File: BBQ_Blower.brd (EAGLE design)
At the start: 84.9 x 75.9 mm, 36 parts, among them IC1 MAX31855RASA+, IC2 MAX31855RASA+, IC3 MAX31855RASA+, J3 PCC-SMP-K-100-R-ROHS, J4 PCC-SMP-K-100-R-ROHS, K1 SRD-12VDC-SL-C, K2 SRD-12VDC-SL-C, Q1 BUZ10, Q2 BUZ10, T1 2N3904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

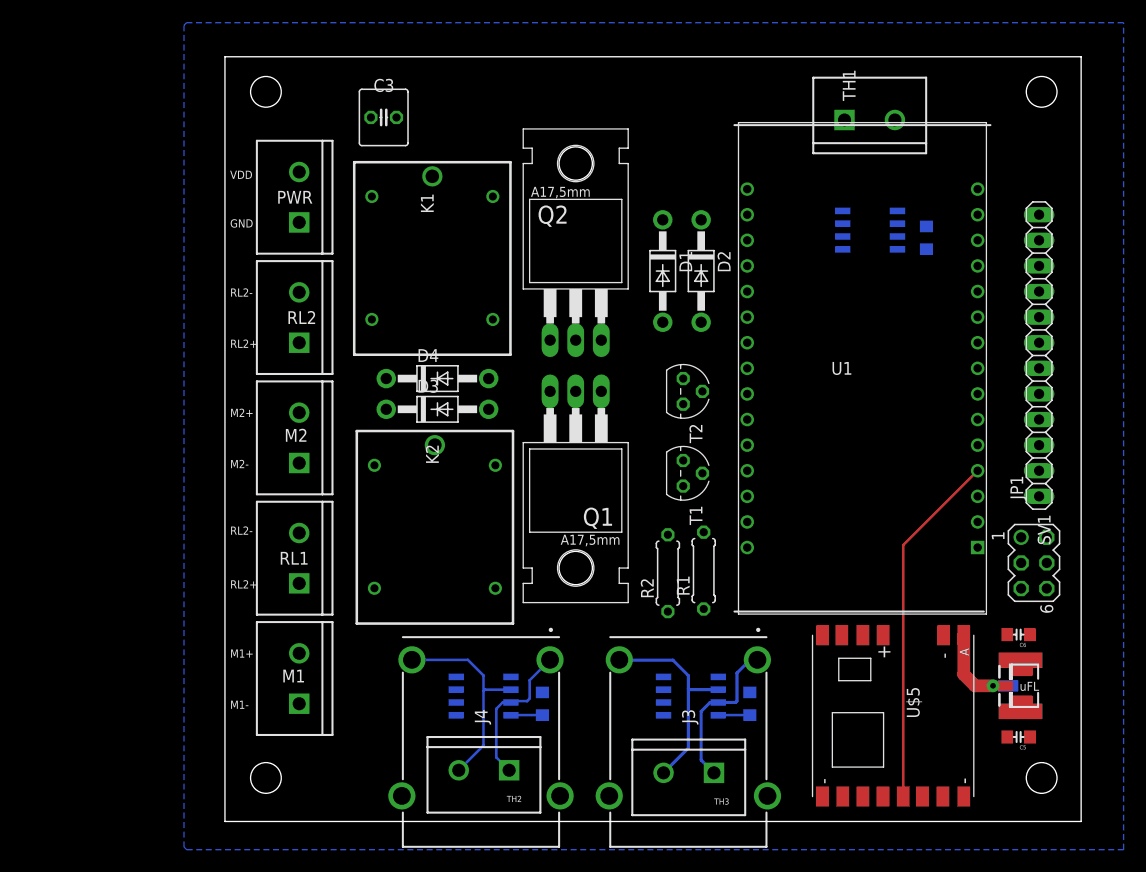
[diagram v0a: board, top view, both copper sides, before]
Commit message: Removed Relay
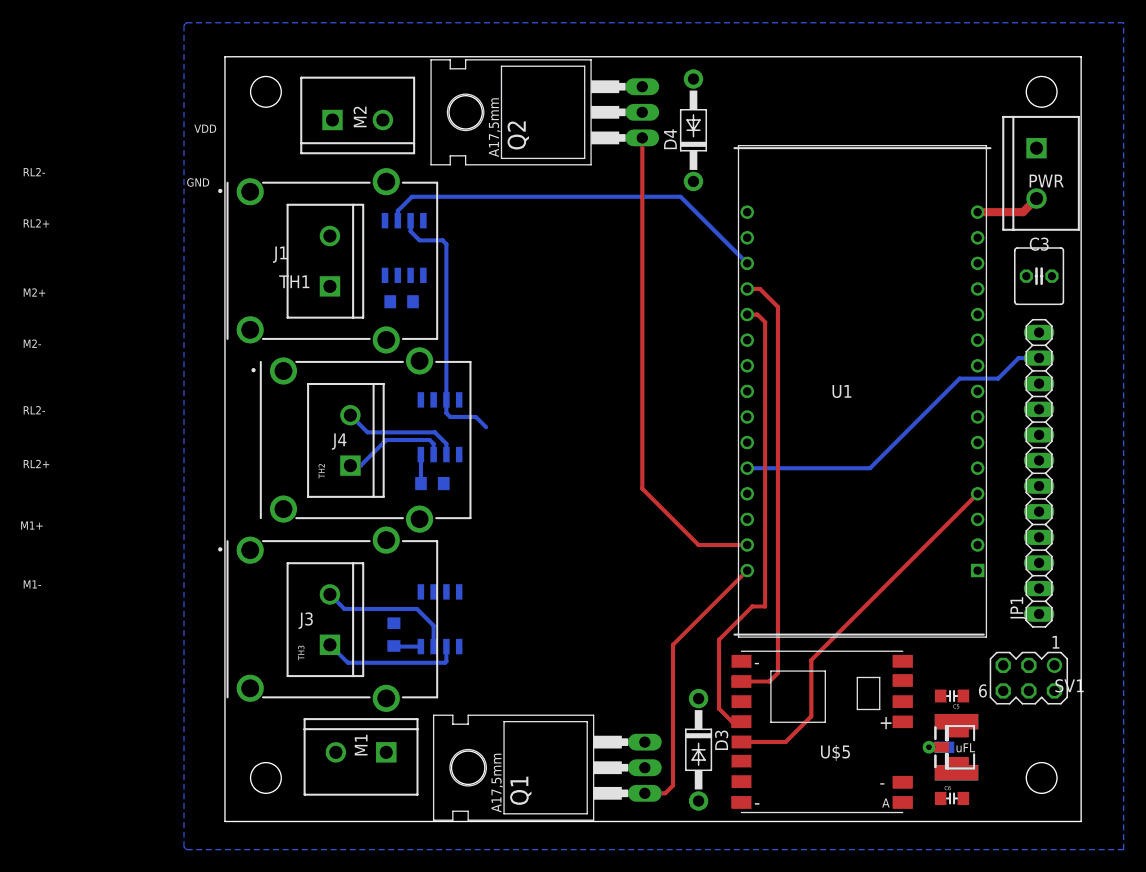
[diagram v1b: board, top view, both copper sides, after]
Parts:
- removed D1, D2: 1N4004, adafruit:DO41-10
- removed K1, K2: SRD-12VDC-SL-C, SRD-12VDC-SL-C:SRD
- removed R1, R2: (no value), resistor:0207/7
- removed RL1, RL2: (no value), SparkFun-Connectors:SCREWTERMINAL-5MM-2
- removed T1, T2: 2N3904, transistor:TO92
- added J1: PCC-SMP-K-100-R-ROHS, PCC-SMP-K-100-R-ROHS:PCC-SMP
- moved PWR 73.5 mm to (85.9, 70.9), turned to 270 degrees
- moved C3 66.9 mm to (86.1, 58.2)
- moved TH1 53.7 mm to (15.7, 57.1), turned to 90 degrees
- moved C7 52.5 mm to (22.9, 55.6), turned to 0 degrees
- moved IC3 46.3 mm to (23.1, 61.0), turned to 90 degrees
- moved J3 45.8 mm to (5.59, 24.1), turned to 0 degrees
- moved D3 42.6 mm to (52.3, 11.2), turned to 270 degrees
- moved TH3 40.2 mm to (15.7, 21.6), turned to 90 degrees
- moved C1 38.3 mm to (25.9, 37.6), turned to 0 degrees
- moved D4 35.4 mm to (51.8, 72.6), turned to 90 degrees
- moved M2 34.2 mm to (16.0, 73.7), turned to 0 degrees
- moved TH2 34.1 mm to (17.8, 39.4), turned to 90 degrees
- moved Q1 31.0 mm to (40.6, 9.40), turned to 90 degrees
- moved J4 29.3 mm to (8.89, 41.9), turned to 0 degrees
- moved IC2 27.0 mm to (26.7, 43.2), turned to 90 degrees
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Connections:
- net GPIO13 renamed SI
- removed net GPIO12: U$5.MISO
- removed net GPIO14: U$5.SCK
- removed net N$1: R1.2, T2.2
- removed net N$2: D1.A, K2.3, T2.1
- removed net N$3: R2.2, T1.2
- removed net N$8: D2.A, K1.3, T1.1
- removed net RELAY1(+): K1.4, RL2.1
- removed net RELAY1(-): K1.1, RL2.2
- removed net RELAY2(+): K2.4, RL1.1
- removed net RELAY2(-): K2.1, RL1.2
- net CS_1: now also U1.22; no longer U1.19
- net CS_3: now also U1.18; no longer U1.22
- net GND: no longer T1.3, T2.3
- net RELAY_1: no longer R2.1
- net RELAY_2: no longer R1.1
- net SCK: now also U$5.SCK
- net SO: now also U$5.MISO, U1.19; no longer U1.18
- net T1+: now also TH3.2; no longer TH3.1
- net T1-: now also TH3.1; no longer TH3.2
- net T3+: now also J1.1
- net T3-: now also J1.2
- net VDD: no longer D1.C, D2.C, K1.2, K2.2
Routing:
- net SO: track 0.00 -> 70.5 mm
- net BLOWER_2: track 0.00 -> 47.5 mm
- net SCK: track 0.00 -> 45.8 mm
- net CS_3: track 0.00 -> 39.0 mm
- net D4: track 0.00 -> 33.5 mm
- net BLOWER_1: track 0.00 -> 27.5 mm
- net T2-: track 20.9 -> 11.8 mm
- net T1-: track 21.2 -> 13.8 mm
- net ANT: track 7.26 -> 0.00 mm
- net VDD: track 0.00 -> 6.40 mm
- net T2+: track 15.0 -> 10.5 mm
- net T1+: track 16.0 -> 13.6 mm
- net CS_LORA: track 35.4 -> 36.9 mm
- net 3V3: track 6.27 -> 5.68 mm

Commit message: traces
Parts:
- moved IC3 3.78 mm to (26.7, 59.7)
- moved C1 3.66 mm to (23.9, 40.6), turned to 270 degrees
- moved IC2 3.45 mm to (30.0, 42.2)
- moved C7 2.74 mm to (21.8, 58.2), turned to 270 degrees
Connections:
- net T2+: now also TH2.2; no longer TH2.1
- net T2-: now also TH2.1; no longer TH2.2
- net T3+: now also TH1.2; no longer TH1.1
- net T3-: now also TH1.1; no longer TH1.2
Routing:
- net 3V3: track 5.68 -> 125.9 mm, vias 0 -> 3
- net VDD: track 6.40 -> 116.5 mm
- net SCK: track 45.8 -> 98.1 mm
- net SO: track 70.5 -> 121.6 mm
- net BLOWER1: track 0.00 -> 47.1 mm
- net CS_1: track 0.00 -> 44.1 mm
- net RST: track 0.00 -> 37.0 mm
- net BLOWER2: track 0.00 -> 35.5 mm
- net CS_2: track 0.00 -> 33.2 mm, vias 0 -> 2
- net T3-: track 0.00 -> 23.8 mm
- net T3+: track 0.00 -> 22.8 mm
- net GND: track 0.00 -> 17.0 mm, vias 0 -> 2
- net ANT: track 0.00 -> 12.5 mm
- net T2-: track 11.8 -> 24.3 mm
- net T2+: track 10.5 -> 22.4 mm
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
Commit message: changed a wire
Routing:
- net CS_2: track 33.2 -> 34.5 mm

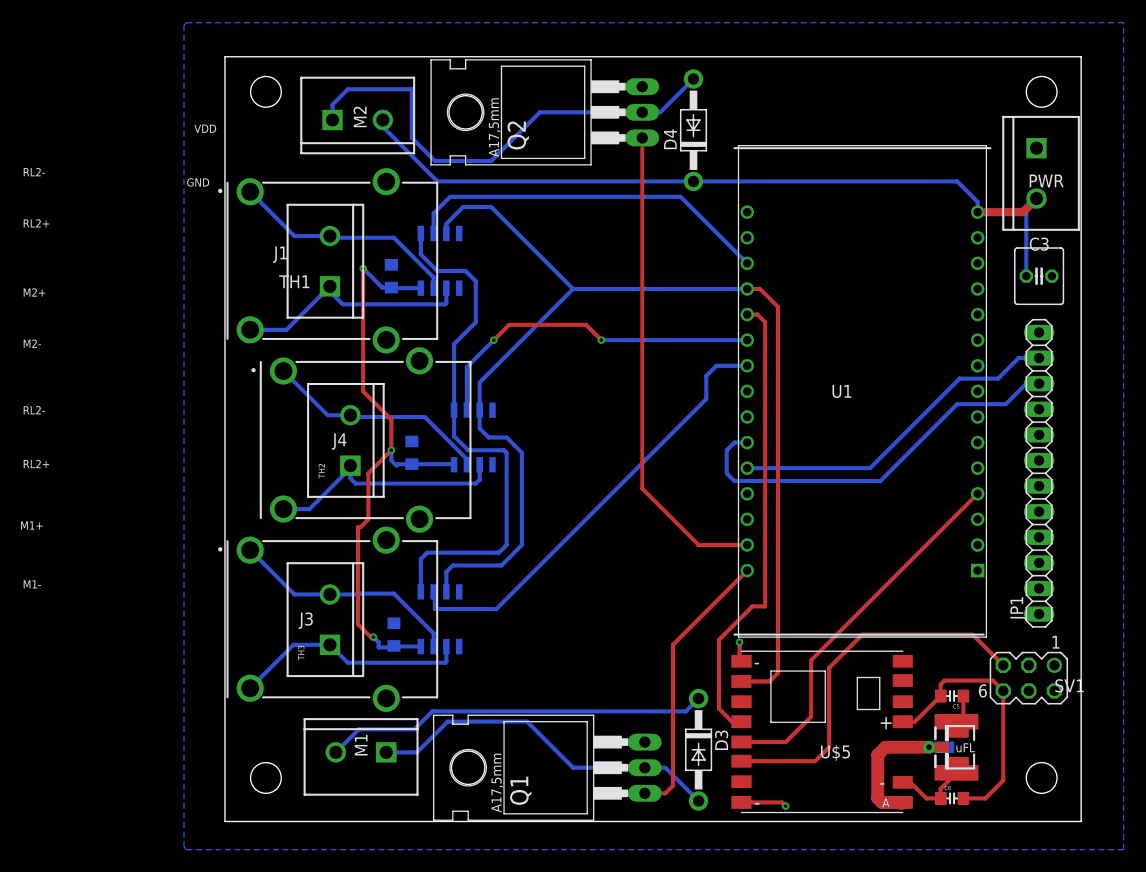
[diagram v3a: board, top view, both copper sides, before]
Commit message: restructured files
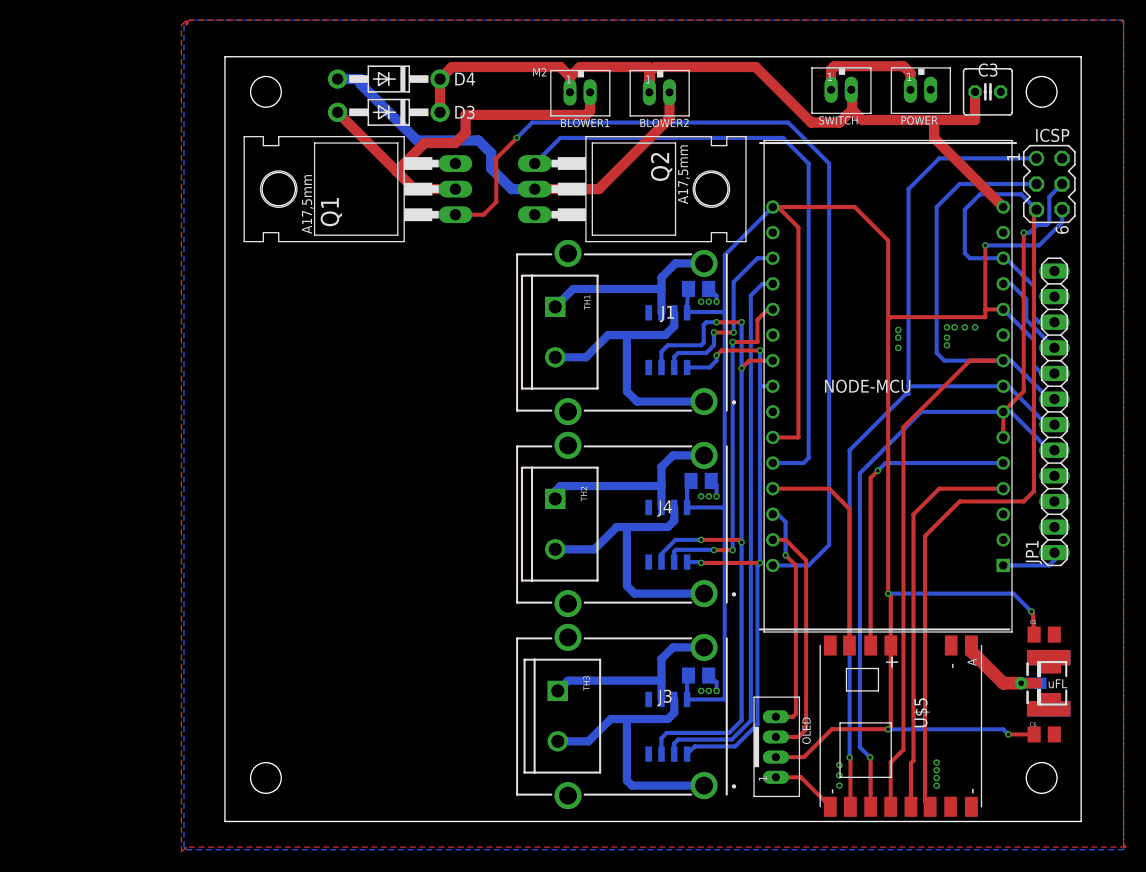
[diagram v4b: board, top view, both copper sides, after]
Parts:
- removed M1, M2, PWR: (no value), SparkFun-Connectors:SCREWTERMINAL-5MM-2
- removed SV1: (no value), con-lstb:MA03-2
- removed U1: 113990105, 113990105:DIP2286W64P254L4826H735Q30N
- added BLOWER1, BLOWER2, POWER, SWITCH: JST-PH_2-PIN_HEADER, SRG:JST_B2B-PH_HEADER
- added ICSP: (no value), con-lstb:MA03-2
- added NODE-MCU: 113990105, 113990105:DIP2286W64P254L4826H735Q30N
- added OLED: JST-PH_4-PIN_HEADER, SRG:JST_B4B-PH_HEADER
- C1, C2, C5, C6, C7: device _c2h:0805-CAP-LARGEPADS -> resistor:C0805K
- C3: value (none) -> 10uF; device adafruit:C025-060X050 -> resistor:C025-050X050
- moved D3 70.3 mm to (21.6, 74.4), turned to 180 degrees
- moved Q1 60.4 mm to (21.8, 66.8)
- moved J3 50.5 mm to (55.1, 14.5), turned to 180 degrees
- moved J1 50.0 mm to (55.1, 52.6), turned to 180 degrees
- moved J4 47.0 mm to (55.1, 33.5), turned to 180 degrees
- moved D4 30.6 mm to (21.6, 77.7), turned to 180 degrees
- moved C7 30.5 mm to (52.3, 56.9), turned to 0 degrees
- moved C2 30.5 mm to (52.3, 18.5), turned to 0 degrees
- moved C1 28.8 mm to (52.6, 37.8), turned to 0 degrees
- moved IC1 25.0 mm to (49.3, 13.5), turned to 270 degrees
- moved IC3 23.9 mm to (49.3, 51.8), turned to 270 degrees
- moved TH3 23.1 mm to (38.4, 17.0), turned to 270 degrees
- moved TH1 22.4 mm to (38.1, 55.1), turned to 270 degrees
- moved IC2 21.6 mm to (49.3, 32.5), turned to 270 degrees
- moved TH2 20.6 mm to (38.1, 36.1), turned to 270 degrees
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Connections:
- removed net CS_1: IC1.6, U1.22
- removed net CS_2: IC2.6, U1.21
- removed net CS_3: IC3.6, U1.18
- removed net GND(1): U1.10
- removed net GND(4): U1.24
- removed net RELAY_1: U1.28
- removed net RELAY_2: U1.27
- removed net SCK: IC1.5, IC2.5, IC3.5, U$5.SCK, U1.20
- removed net SI: U$5.MOSI
- removed net SO: IC1.7, IC2.7, IC3.7, U$5.MISO, U1.19
- removed net SO_1: U1.23
- removed net VDD3V3(1): U1.11
- new net CS_BBQ: IC3.6, NODE-MCU.18
- new net CS_TF1: IC1.6, NODE-MCU.19
- new net CS_TF2: IC2.6, NODE-MCU.20
- new net DIO5: U$5.DIO5
- new net HMISO: IC1.7, IC2.7, IC3.7, NODE-MCU.22
- new net HMOSI: NODE-MCU.21
- new net HSCK: IC1.5, IC2.5, IC3.5, NODE-MCU.23
- new net SCL: NODE-MCU.29, OLED.P3
- new net SDA: NODE-MCU.28, OLED.P4
- new net VIN: POWER.P1, SWITCH.P1
- net 3V3: now also ICSP.6, JP1.8, NODE-MCU.11, NODE-MCU.16, NODE-MCU.25, OLED.P2; no longer JP1.10, SV1.6, U1.16, U1.25
- net A0: now also NODE-MCU.1; no longer U1.1
- net BLOWER1: now also BLOWER2.P2; no longer M2.1
- net BLOWER2: now also BLOWER1.P2; no longer M1.1
- net BLOWER_1: now also NODE-MCU.30; no longer U1.30
- net BLOWER_2: now also NODE-MCU.26; no longer U1.29
- net CLK: now also ICSP.3, NODE-MCU.9, U$5.SCK; no longer SV1.3, U1.9
- net CS_LORA: now also NODE-MCU.4; no longer U1.4
- net D1: no longer U1.6
- net D2: no longer U1.5
- net D4: no longer U1.26
- net DIO0: now also NODE-MCU.5
- net DIO1: now also NODE-MCU.27
- net EN: now also JP1.9, NODE-MCU.12; no longer JP1.8, U1.12
- net GND: now also ICSP.2, NODE-MCU.10, NODE-MCU.14, NODE-MCU.17, NODE-MCU.24, OLED.P1, POWER.P2; no longer PWR.1, SV1.2, U1.14, U1.17
- net MISO: now also ICSP.1, NODE-MCU.8, U$5.MISO; no longer SV1.1, U1.8
- net MOSI: now also ICSP.4, NODE-MCU.6, NODE-MCU.7, U$5.MOSI; no longer SV1.4, U1.7
- net RST: now also ICSP.5, JP1.10, NODE-MCU.13; no longer JP1.9, SV1.5, U1.13
- net VDD: now also BLOWER1.P1, BLOWER2.P1, NODE-MCU.15, SWITCH.P2; no longer M1.2, M2.2, PWR.2, U1.15
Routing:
- net SO: track 121.6 -> 0.00 mm
- net 3V3: track 125.9 -> 240.1 mm, vias 3 -> 5
- net SCK: track 98.1 -> 0.00 mm
- net MISO: track 0.00 -> 93.9 mm, vias 0 -> 1
- net CLK: track 0.00 -> 89.7 mm
- net MOSI: track 0.00 -> 85.4 mm, vias 0 -> 2
- net HMISO: track 0.00 -> 74.4 mm, vias 0 -> 5
- net HSCK: track 0.00 -> 62.2 mm, vias 0 -> 4
- net BLOWER_1: track 27.5 -> 89.4 mm, vias 0 -> 1
- net RST: track 37.0 -> 94.0 mm
- net CS_TF1: track 0.00 -> 54.4 mm
- net CS_1: track 44.1 -> 0.00 mm
- net CS_3: track 36.5 -> 0.00 mm
- net CS_2: track 34.5 -> 0.00 mm, vias 2 -> 0
- net CS_TF2: track 0.00 -> 34.2 mm, vias 0 -> 3
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- added copper zone on layer 1, net GND
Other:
- board text added: "+"
- board text added: "-"
- board text added: "BBQ Temp"
- board text added: "Board: BBQ Controller Author: Cody Fischer Date: August 2019 Rev: 1.0"
- board text added: "Food Temp 1"
- board text added: "Food Temp 2"
- board text added: "M2"
- board text removed: "Board: BBQ Controller Author: Cody Fischer Date: November 2018 Rev: 1.0"
- board text removed: "GND"
- board text removed: "M1+"
- board text removed: "M1-"
- board text removed: "M2+"
- board text removed: "M2-"
- board text removed: "RL2+"
- board text removed: "RL2-"
- board text removed: "VDD"

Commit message: cleaned structure
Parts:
- moved POWER 2.03 mm to (72.4, 76.7)
- moved C3 1.78 mm to (79.2, 76.5)
- moved SWITCH 0.76 mm to (65.8, 76.7)
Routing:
- net VDD: track 84.9 -> 83.4 mm
- net VIN: track 11.9 -> 10.6 mm
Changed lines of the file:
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@@
 </autorouter>
 <elements>
-<element name="C3" library="resistor" library_urn="urn:adsk.eagle:library:348" package="C025-050X050" package3d_urn="urn:adsk.eagle:package:26152/1" value="10uF" x="81.026" y="76.454" smashed="yes">
-<attribute name="NAME" x="80.01" y="77.978" size="1.27" layer="25" ratio="10"/>
-<attribute name="VALUE" x="78.994" y="74.041" size="1.27" layer="27" ratio="10"/>
+<element name="C3" library="resistor" library_urn="urn:adsk.eagle:library:348" package="C025-050X050" package3d_urn="urn:adsk.eagle:package:26152/1" value="10uF" x="79.248" y="76.454" smashed="yes">
+<attribute name="NAME" x="78.232" y="77.978" size="1.27" layer="25" ratio="10"/>
+<attribute name="VALUE" x="77.216" y="74.041" size="1.27" layer="27" ratio="10"/>
 </element>
 <element name="D3" library="adafruit" package="DO41-10" value="1N4004" x="21.59" y="74.422" smashed="yes" rot="R180">
@@
 <attribute name="SUPPLIER_NAME" value="RS" x="57.658" y="52.578" size="1.778" layer="27" rot="R180" display="off"/>
 </element>
-<element name="POWER" library="SRG" package="JST_B2B-PH_HEADER" value="JST-PH_2-PIN_HEADER" x="74.422" y="76.708" smashed="yes" rot="R180">
-<attribute name="NAME" x="76.077" y="74.0255" size="0.8128" layer="25" font="vector" rot="R180"/>
+<element name="POWER" library="SRG" package="JST_B2B-PH_HEADER" value="JST-PH_2-PIN_HEADER" x="72.39" y="76.708" smashed="yes" rot="R180">
+<attribute name="NAME" x="74.045" y="74.0255" size="0.8128" layer="25" font="vector" rot="R180"/>
 </element>
 <element name="BLOWER2" library="SRG" package="JST_B2B-PH_HEADER" value="JST-PH_2-PIN_HEADER" x="48.514" y="76.454" smashed="yes" rot="R180">
@@
 <attribute name="NAME" x="62.6265" y="14.45" size="0.8128" layer="25" font="vector" rot="R270"/>
 </element>
-<element name="SWITCH" library="SRG" package="JST_B2B-PH_HEADER" value="JST-PH_2-PIN_HEADER" x="66.548" y="76.708" smashed="yes" rot="R180">
-<attribute name="NAME" x="68.203" y="74.0255" size="0.8128" layer="25" font="vector" rot="R180"/>
+<element name="SWITCH" library="SRG" package="JST_B2B-PH_HEADER" value="JST-PH_2-PIN_HEADER" x="65.786" y="76.708" smashed="yes" rot="R180">
+<attribute name="NAME" x="67.441" y="74.0255" size="0.8128" layer="25" font="vector" rot="R180"/>
 </element>
 </elements>
@@
 <contactref element="BLOWER2" pad="P1"/>
 <contactref element="BLOWER1" pad="P1"/>
-<wire x1="79.756" y1="76.454" x2="79.756" y2="73.66" width="1.016" layer="1"/>
+<wire x1="77.978" y1="76.454" x2="77.978" y2="73.66" width="1.016" layer="1"/>
 <wire x1="75.692" y1="73.66" x2="75.692" y2="71.882" width="1.016" layer="1"/>
-<wire x1="75.692" y1="73.66" x2="79.756" y2="73.66" width="1.016" layer="1"/>
+<wire x1="75.692" y1="73.66" x2="77.978" y2="73.66" width="1.016" layer="1"/>
 <wire x1="48.006" y1="78.918" x2="57.988" y2="78.918" width="1.016" layer="1"/>
 <wire x1="48.006" y1="78.918" x2="47.439" y2="78.351" width="1.016" layer="1"/>
@@
 <contactref element="SWITCH" pad="P2"/>
 <wire x1="66.294" y1="73.406" x2="67.564" y2="74.676" width="1.016" layer="1"/>
-<wire x1="67.564" y1="76.5695" x2="67.473" y2="76.6605" width="1.016" layer="1"/>
+<wire x1="67.564" y1="75.8075" x2="66.711" y2="76.6605" width="1.016" layer="1"/>
 <wire x1="57.988" y1="78.918" x2="63.5" y2="73.406" width="1.016" layer="1"/>
 <wire x1="63.5" y1="73.406" x2="66.294" y2="73.406" width="1.016" layer="1"/>
-<wire x1="67.564" y1="74.676" x2="67.564" y2="76.5695" width="1.016" layer="1"/>
+<wire x1="67.564" y1="74.676" x2="67.564" y2="75.8075" width="1.016" layer="1"/>
 <wire x1="75.692" y1="73.66" x2="68.58" y2="73.66" width="1.016" layer="1"/>
 <wire x1="68.58" y1="73.66" x2="67.564" y2="74.676" width="1.016" layer="1"/>
@@
 <contactref element="SWITCH" pad="P1"/>
 <contactref element="POWER" pad="P1"/>
-<wire x1="65.473" y1="76.6605" x2="65.473" y2="78.681" width="1.016" layer="1"/>
-<wire x1="65.473" y1="78.681" x2="65.786" y2="78.994" width="1.016" layer="1"/>
-<wire x1="65.786" y1="78.994" x2="72.644" y2="78.994" width="1.016" layer="1"/>
-<wire x1="73.347" y1="78.291" x2="73.347" y2="76.6605" width="1.016" layer="1"/>
-<wire x1="72.644" y1="78.994" x2="73.347" y2="78.291" width="1.016" layer="1"/>
+<wire x1="64.711" y1="76.6605" x2="64.711" y2="77.919" width="1.016" layer="1"/>
+<wire x1="64.711" y1="77.919" x2="65.786" y2="78.994" width="1.016" layer="1"/>
+<wire x1="65.786" y1="78.994" x2="71.315" y2="78.994" width="1.016" layer="1"/>
+<wire x1="71.315" y1="78.994" x2="71.315" y2="76.6605" width="1.016" layer="1"/>
 </signal>
 </signals>
